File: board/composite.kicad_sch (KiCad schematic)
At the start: 24 parts, among them J10 VGA, J5 VIDEO_JTAG_BYPASS, J6 COMPOSITE, U17 VIDEO, Y1 14.318MHz, Y3 25.175MHz

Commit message: update parts I've added
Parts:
- removed C16: 100nF, Capacitor_THT:C_Disc_D5.0mm_W2.5mm_P5.00mm, symbol Device:C
- removed U17: VIDEO, Package_LCC:PLCC-84_THT-Socket, symbol CPLD_Microchip:ATF1508ASx-xxJx84
- removed Y1: 14.318MHz, Oscillator:Oscillator_DIP-8, symbol Oscillator:CXO_DIP8
- added U18: ATF1504AS-xAx44, Package_QFP:TQFP-44_10x10mm_P0.8mm, symbol CPLD_Microchip:ATF1504AS-xAx44
- Y3: Datasheet-rev1 (none) -> http://cdn-reichelt.de/documents/datenblatt/B400/OSZI.pdf; Digikey https://www.digikey.com/en/products/detail/shenzhen-sctf-el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 -> https://www.digikey.com/en/products/detail/ecs-inc/ECS-100A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
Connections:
- net +5V: now also U18.17 (VCC), U18.29 (VCC), U18.41 (VCC), U18.9 (VCC)
- net VGA_CLK_ENB: no longer names the net of Y3.1 (EN)
- new net: U18.16 (GND), U18.24 (GND), U18.36 (GND), U18.4 (GND)
- no-connect marks 21 -> 6

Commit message: checkpoint
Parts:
- removed C35: 220µF, Capacitor_THT:CP_Radial_D6.3mm_P2.50mm, symbol Device:C
- removed J10: VGA, board:AMPHENOL_ICD15S13E4GX00LF, symbol HD15:ICD15S13E4GX00LF
- removed J5: VIDEO_JTAG_BYPASS, Connector_PinHeader_2.54mm:PinHeader_1x02_P2.54mm_Vertical, symbol Connector:Conn_01x02_Pin
- removed J6: COMPOSITE, board:CUI_RCJ-044, symbol Connector:Conn_Coaxial
- removed R14: 1K, Resistor_THT:R_Axial_DIN0207_L6.3mm_D2.5mm_P10.16mm_Horizontal, symbol Device:R
- removed R16: 33, Resistor_THT:R_Axial_DIN0207_L6.3mm_D2.5mm_P10.16mm_Horizontal, symbol Device:R
- removed R20, R26: 560, Resistor_THT:R_Axial_DIN0207_L6.3mm_D2.5mm_P10.16mm_Horizontal, symbol Device:R
- removed R21, R25, R31: 270, Resistor_THT:R_Axial_DIN0207_L6.3mm_D2.5mm_P10.16mm_Horizontal, symbol Device:R
- removed R22, R23: 1100, Resistor_THT:R_Axial_DIN0207_L6.3mm_D2.5mm_P10.16mm_Horizontal, symbol Device:R
- removed R40, R41, R42: 150, Resistor_THT:R_Axial_DIN0207_L6.3mm_D2.5mm_P10.16mm_Horizontal, symbol Device:R_Small
- added C16: 100nF, Capacitor_THT:C_Disc_D5.0mm_W2.5mm_P5.00mm, symbol Device:C
- added Y1: OSC2, Oscillator:Oscillator_DIP-8, symbol Oscillator:CXO_DIP8
- R12: value 560 -> 100K; Package 0603 -> (none); Type SMD -> (none)
- R15: value 430 -> 100K
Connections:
- net CPST_PIXEL is gone; now on net +5V: R15.1
- net VGA_B0 is gone; now on an unnamed net: R12.2
- net VGA_BLUE is gone; now on net +5V: R12.1
- net +5V: now also C16.1, Y1.8 (Vcc)
- net GND: now also U18.16 (GND), U18.24 (GND), U18.36 (GND), U18.4 (GND), C16.2, Y1.4 (GND)
- net at R15.2: now also Y1.1 (EN)
- new net CLK2: Y1.5 (OUT)
- no-connect marks 6 -> 0
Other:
- note added: "Datasheet oscillators are NC on pin 1 but some of my oscillators in hand are ENB on pin 1, so pull-up as a hedge"
- moved on the sheet: C30

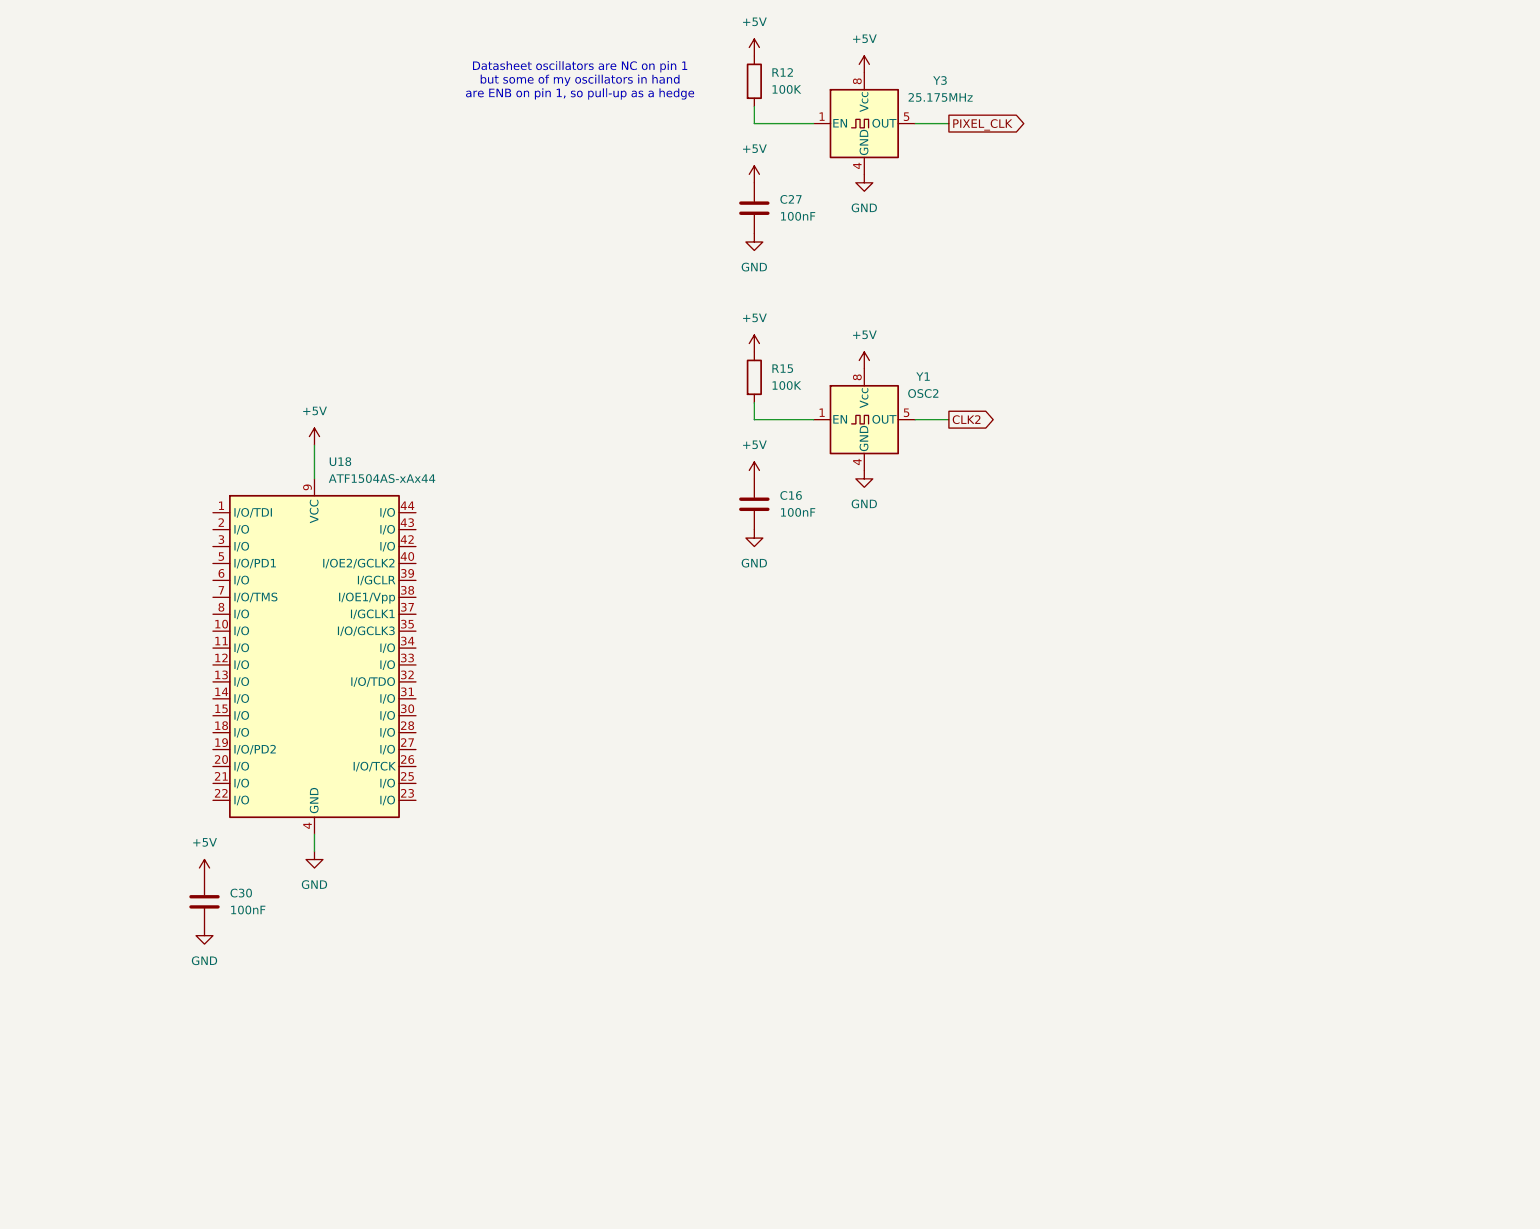
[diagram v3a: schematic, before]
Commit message: capture ENGINE in schematic; fix couple of shorts
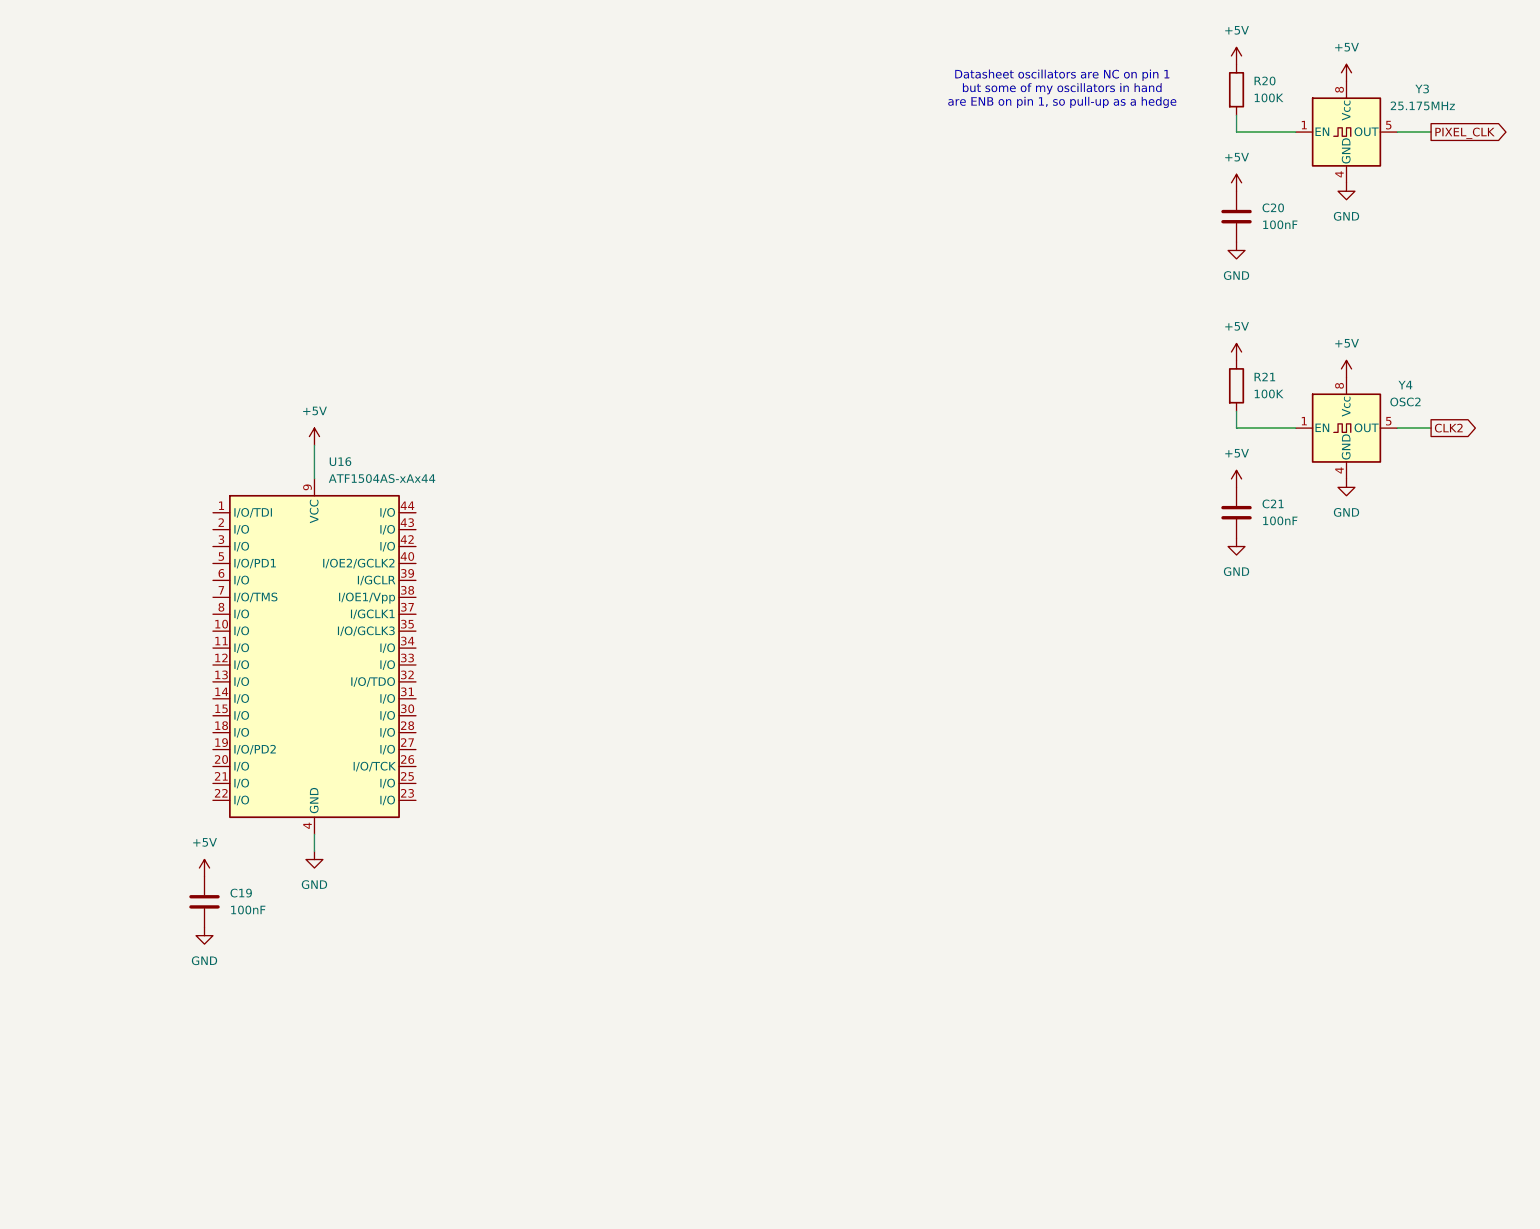
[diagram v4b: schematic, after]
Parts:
- renumbered C30 to C19, C27 to C20, C16 to C21, R12 to R20, R15 to R21, U18 to U16, Y1 to Y4
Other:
- moved on the sheet: C20, C21, R20, R21, Y3, Y4
